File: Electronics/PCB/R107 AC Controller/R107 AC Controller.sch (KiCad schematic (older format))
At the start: 54 parts, among them J1 CAR 12V, J2 CAR GND, J3 COMPRESSOR, J4 BLOWER, J5 KNOB, J6 THERMOCOUPLE, J7 USB_B_Mini, J8 ISP, K1 G5LE-1, K2 G5LE-1, Q1 MMBT2222, Q2 MMBT2222, U1 ATmega328P, U2 MPM3610, U3 MAX31855KASA, U4 FT232RL, Y1 16MHz

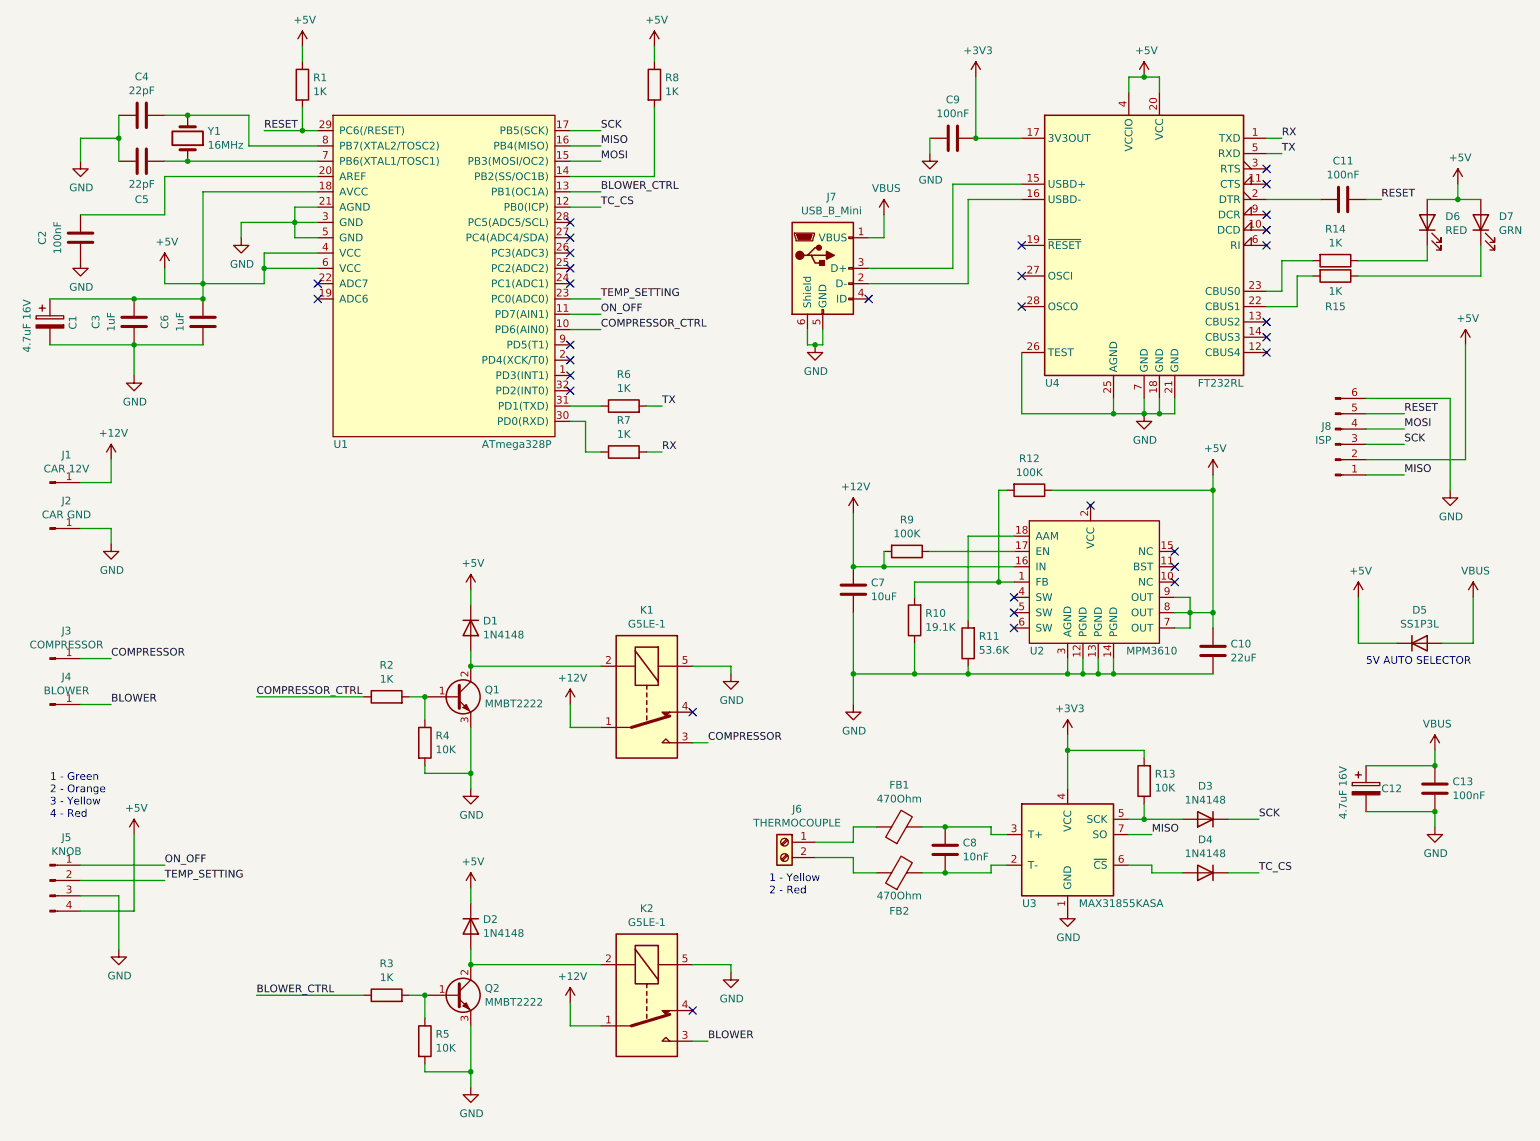
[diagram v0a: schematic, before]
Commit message: Updated schematic to fix mistakes.
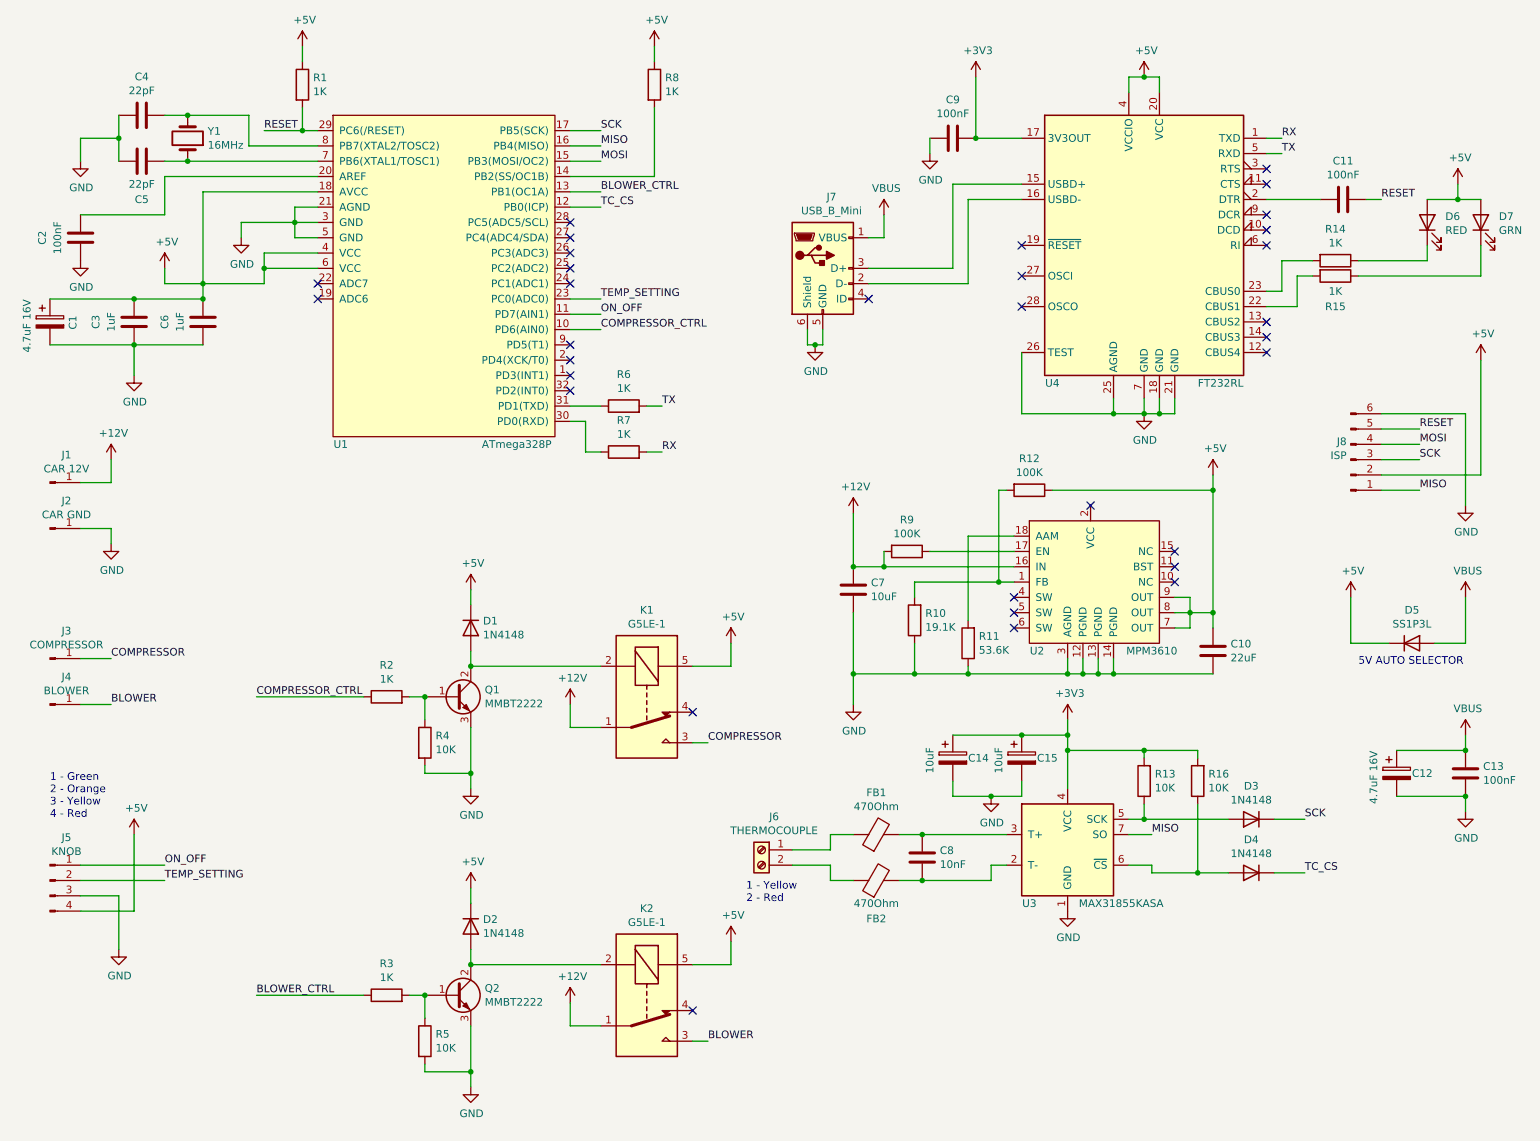
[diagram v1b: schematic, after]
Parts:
- added C14, C15: 10uF, symbol Device:CP
- added R16: 10K, symbol Device:R
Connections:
- net +3V3: now also C14.1, C15.1, R16.2
- net +5V: now also K1.5, K2.5
- net GND: now also C14.2, C15.2; no longer K1.5, K2.5
- net at D4.2 (A), U3.6 (~CS~): now also R16.1
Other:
- moved on the sheet: C12, C13, C8, D3, D4, D5, FB1, FB2, J6, J8

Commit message: Updated schematic. Added BOM. Added more data sheets.
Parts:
- removed C10: 22uF, symbol Device:C
- removed C7: 10uF, symbol Device:C
- removed J1: CAR 12V, symbol Connector:Conn_01x01_Male
- removed J2: CAR GND, symbol Connector:Conn_01x01_Male
- removed J3: COMPRESSOR, symbol Connector:Conn_01x01_Male
- removed J4: BLOWER, symbol Connector:Conn_01x01_Male
- removed R10: 19.1K, symbol Device:R
- removed R11: 53.6K, symbol Device:R
- removed R12, R9: 100K, symbol Device:R
- removed U2: MPM3610, symbol BritishIdeas:MPM3610
- added C12: 220uF e, Capacitor_SMD:CP_Elec_8x6.5, symbol Device:CP
- added C7: 680uF e, Capacitor_SMD:CP_Elec_10x10.5, symbol Device:CP
- added D3: SK34ATR, Diode_SMD:D_SMA, symbol Device:D_Schottky
- added J1: CAR POWER, Britishideas:Keystone_SturdiMount_TabConnector_1x2, symbol Connector_Generic:Conn_01x02
- added J2: CONTROL, Britishideas:Keystone_SturdiMount_TabConnector_1x2, symbol Connector_Generic:Conn_01x02
- added J3: ACCESSORY, Connector_PinHeader_2.54mm:PinHeader_2x03_P2.54mm_Vertical, symbol Connector_Generic:Conn_01x06
- added JP1: OPT1, Connector_PinHeader_2.54mm:PinHeader_1x02_P2.54mm_Vertical, symbol Connector_Generic:Conn_01x02
- added JP2: OPT2, Connector_PinHeader_2.54mm:PinHeader_1x02_P2.54mm_Vertical, symbol Connector_Generic:Conn_01x02
- added L1: 33uH, Britishideas:Chilisin_Power_Inductor_AWVS, symbol Device:L
- added U2: LM2596S-5, Package_TO_SOT_SMD:TO-263-5_TabPin3, symbol Regulator_Switching:LM2596S-5
- C1: value 4.7uF 16V -> 4.7uF e; footprint (none) -> Capacitor_SMD:CP_Elec_4x5.8
- C10: renamed from C14; value 10uF -> 10uF e; footprint (none) -> Capacitor_SMD:CP_Elec_4x5.4
- C11: renamed from C15; value 10uF -> 10uF e; footprint (none) -> Capacitor_SMD:CP_Elec_4x5.4
- C13: renamed from C11; footprint (none) -> Capacitor_SMD:C_0805_2012Metric
- C14: renamed from C12; value 4.7uF 16V -> 4.7uF 16V e; footprint (none) -> Capacitor_SMD:CP_Elec_4x5.8
- C15: renamed from C13; footprint (none) -> Capacitor_SMD:C_0805_2012Metric
- C2, C3, C6, C8, C9: footprint (none) -> Capacitor_SMD:C_0805_2012Metric
- C4, C5: value 22pF -> 18pF; footprint (none) -> Capacitor_SMD:C_0805_2012Metric
- D1, D2: value 1N4148 -> MMSD4148T1G; footprint (none) -> Diode_SMD:D_SOD-123
- D4: renamed from D3; value 1N4148 -> MMSD4148T1G; footprint (none) -> Diode_SMD:D_SOD-123
- D5: renamed from D4; value 1N4148 -> MMSD4148T1G; footprint (none) -> Diode_SMD:D_SOD-123
- D6: renamed from D5; value SS1P3L -> SS1P3L-M3/84A; footprint (none) -> Britishideas:SMP_DO-220AA
- D7: renamed from D6; footprint (none) -> LED_SMD:LED_PLCC-2
- D8: renamed from D7; footprint (none) -> LED_SMD:LED_PLCC-2
- FB1, FB2: value 470Ohm -> BLM21AG471SH1D; footprint (none) -> Inductor_SMD:L_0805_2012Metric
- J4: renamed from J5; footprint (none) -> Britishideas:Keystone_SturdiMount_TabConnector_1x4; symbol Connector:Conn_01x04_Male -> Connector_Generic:Conn_01x04
- J5: renamed from J6; footprint (none) -> TerminalBlock_TE-Connectivity:TerminalBlock_TE_282834-2_1x02_P2.54mm_Horizontal
- J6: renamed from J7; footprint (none) -> Connector_USB:USB_Mini-B_Wuerth_65100516121_Horizontal
- J7: renamed from J8; footprint (none) -> Connector_PinHeader_2.54mm:PinHeader_2x03_P2.54mm_Vertical; symbol Connector:Conn_01x06_Male -> Connector_Generic:Conn_01x06
- Q1, Q2: value MMBT2222 -> MMBT2222ALT1G; footprint (none) -> Package_TO_SOT_SMD:SOT-23; symbol Device:Q_NPN_BCE -> Device:Q_NPN_BEC
- R1, R2, R3, R4, R5, R6, R7, R8: footprint (none) -> Resistor_SMD:R_0805_2012Metric
- R10: renamed from R16; footprint (none) -> Resistor_SMD:R_0805_2012Metric
- R11: renamed from R14; footprint (none) -> Resistor_SMD:R_0805_2012Metric
- R12: renamed from R15; footprint (none) -> Resistor_SMD:R_0805_2012Metric
- R9: renamed from R13; footprint (none) -> Resistor_SMD:R_0805_2012Metric
- U1: footprint (none) -> Package_QFP:LQFP-32_7x7mm_P0.8mm
- Y1: value 16MHz -> ECS-160-18-5PX-TR 16MHz; footprint (none) -> Britishideas:HC-49_US
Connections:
- net +12V: now also C7.1, J1.1 (Pin_1), U2.1 (VIN)
- net +5V: now also C12.1, J3.1 (Pin_1), L1.2, U2.4 (FB)
- net BLOWER: now also J2.2 (Pin_2)
- net BLOWER_CTRL: now also J3.2 (Pin_2)
- net COMPRESSOR: now also J2.1 (Pin_1)
- net COMPRESSOR_CTRL: now also J3.3 (Pin_3)
- net GND: now also Q1.2 (E), Q2.2 (E), C12.2, C7.2, D3.2 (A), J1.2 (Pin_2), J3.6 (Pin_6), JP1.2 (Pin_2), JP2.2 (Pin_2), U2.3 (GND), U2.5 (~ON~/OFF); no longer Q1.3 (E), Q2.3 (E)
- net ON_OFF: now also J3.5 (Pin_5)
- net TEMP_SETTING: now also J3.4 (Pin_4)
- net at U1.27 (PC4(ADC4/SDA)): now also JP1.1 (Pin_1)
- net at U1.28 (PC5(ADC5/SCL)): now also JP2.1 (Pin_1)
- net at D1.2 (A), K1.2: now also Q1.3 (C); no longer Q1.2 (C)
- net at D2.2 (A), K2.2: now also Q2.3 (C); no longer Q2.2 (C)
- new net: D3.1 (K), L1.1, U2.2 (OUT)
- no-connect marks 32 -> 23

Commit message: Improvements to schematic. Started work on PCB.
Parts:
- J3: footprint Connector_PinHeader_2.54mm:PinHeader_2x03_P2.54mm_Vertical -> Connector_PinHeader_2.54mm:PinHeader_1x07_P2.54mm_Vertical; symbol Connector_Generic:Conn_01x06 -> Connector_Generic:Conn_01x07
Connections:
- net GND: now also J3.7 (Pin_7); no longer J3.6 (Pin_6)
- net ACC_IO: now reaches U1.24 (PC1(ADC1))
- net ACC_IO: now also J3.6 (Pin_6)
- no-connect marks 23 -> 22
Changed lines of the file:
@@
 NoConn ~ 2550 2400
 NoConn ~ 2550 2500
-NoConn ~ 4200 2400
 NoConn ~ 4200 2300
 NoConn ~ 4200 2200
@@
 	4300 7250 4300 7100
 $Comp
-L Connector_Generic:Conn_01x06 J3
+L Connector_Generic:Conn_01x07 J3
 U 1 1 5FFD8007
-P 800 5900
-F 0 "J3" H 718 6317 50  0000 C CNN
-F 1 "ACCESSORY" H 718 6226 50  0000 C CNN
-F 2 "Connector_PinHeader_2.54mm:PinHeader_2x03_P2.54mm_Vertical" H 800 5900 50  0001 C CNN
-F 3 "~" H 800 5900 50  0001 C CNN
-	1    800  5900
+P 800 5850
+F 0 "J3" H 800 6350 50  0000 C CNN
+F 1 "ACCESSORY" H 800 6250 50  0000 C CNN
+F 2 "Connector_PinHeader_2.54mm:PinHeader_1x07_P2.54mm_Vertical" H 800 5850 50  0001 C CNN
+F 3 "~" H 800 5850 50  0001 C CNN
+	1    800  5850
 	-1   0    0    -1
 $EndComp
 Wire Wire Line
-	1000 5800 1200 5800
-Wire Wire Line
-	1000 5900 1200 5900
-Text Label 1200 5800 0    50   ~ 0
+	1000 5650 1200 5650
+Wire Wire Line
+	1000 5750 1200 5750
+Text Label 1200 5650 0    50   ~ 0
 BLOWER_CTRL
-Text Label 1200 5900 0    50   ~ 0
+Text Label 1200 5750 0    50   ~ 0
 COMPRESSOR_CTRL
 $Comp
@@
 	5050 1450 5050 2000
 Wire Wire Line
-	1000 6000 1200 6000
-Wire Wire Line
-	1000 6100 1200 6100
-Text Label 1200 6000 0    50   ~ 0
+	1000 5850 1200 5850
+Wire Wire Line
+	1000 5950 1200 5950
+Text Label 1200 5850 0    50   ~ 0
 TEMP_SETTING
-Text Label 1200 6100 0    50   ~ 0
+Text Label 1200 5950 0    50   ~ 0
 ON_OFF
 $Comp
 L power:+5V #PWR03
 U 1 1 600B026C
-P 1150 5500
-F 0 "#PWR03" H 1150 5350 50  0001 C CNN
-F 1 "+5V" H 1165 5673 50  0000 C CNN
-F 2 "" H 1150 5500 50  0001 C CNN
-F 3 "" H 1150 5500 50  0001 C CNN
-	1    1150 5500
+P 1150 5350
+F 0 "#PWR03" H 1150 5200 50  0001 C CNN
+F 1 "+5V" H 1165 5523 50  0000 C CNN
+F 2 "" H 1150 5350 50  0001 C CNN
+F 3 "" H 1150 5350 50  0001 C CNN
+	1    1150 5350
 	1    0    0    -1
 $EndComp
@@
 L power:GND #PWR04
 U 1 1 600B0669
-P 1150 6400
-F 0 "#PWR04" H 1150 6150 50  0001 C CNN
-F 1 "GND" H 1155 6227 50  0000 C CNN
-F 2 "" H 1150 6400 50  0001 C CNN
-F 3 "" H 1150 6400 50  0001 C CNN
-	1    1150 6400
-	1    0    0    -1
-$EndComp
-Wire Wire Line
-	1150 5500 1150 5700
-Wire Wire Line
-	1150 5700 1000 5700
-Wire Wire Line
-	1000 6200 1150 6200
-Wire Wire Line
-	1150 6200 1150 6400
+P 1150 6350
+F 0 "#PWR04" H 1150 6100 50  0001 C CNN
+F 1 "GND" H 1155 6177 50  0000 C CNN
+F 2 "" H 1150 6350 50  0001 C CNN
+F 3 "" H 1150 6350 50  0001 C CNN
+	1    1150 6350
+	1    0    0    -1
+$EndComp
+Wire Wire Line
+	1150 5350 1150 5550
+Wire Wire Line
+	1150 5550 1000 5550
 $Comp
 L Connector_Generic:Conn_01x02 J1
@@
 Text Label 1200 4850 0    50   ~ 0
 BLOWER
+Wire Wire Line
+	4200 2400 4400 2400
+Text Label 4400 2400 0    50   ~ 0
+ACC_IO
+Wire Wire Line
+	1000 6150 1150 6150
+Wire Wire Line
+	1150 6150 1150 6350
+Wire Wire Line
+	1000 6050 1200 6050
+Text Label 1200 6050 0    50   ~ 0
+ACC_IO
 $EndSCHEMATC
